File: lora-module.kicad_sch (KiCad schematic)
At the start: 10 parts, among them J101 Conn_Coaxial, J102 Conn_ARM_SWD_TagConnect_TC203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, Q101 PMN48XP

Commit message: added teardrops, finishing touches
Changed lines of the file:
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@@
     (in_bom no) (on_board yes) (dnp no) (fields_autoplaced)
     (property "Reference" "J106" (at 45.72 116.5169 0)
-      (effects (font (size 1.27 1.27)))
+      (effects (font (size 1.27 1.27)) hide)
     )
     (property "Value" "~" (at 45.72 116.84 0)

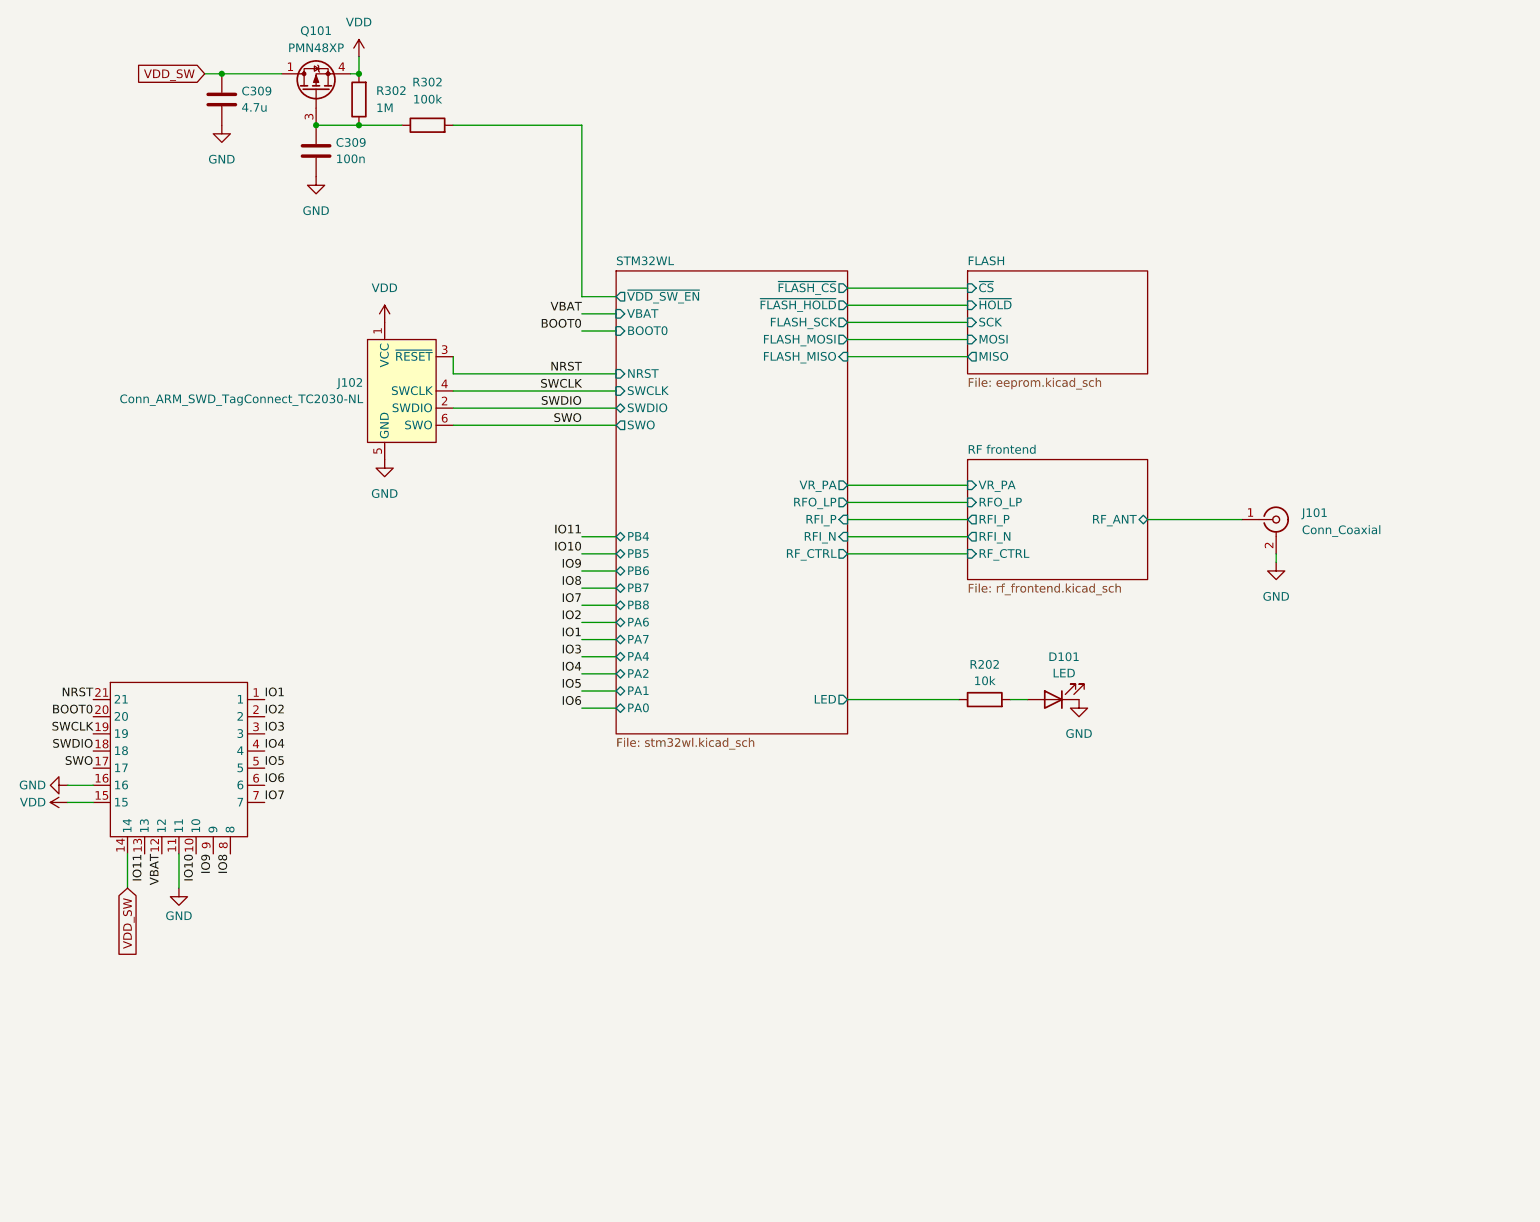
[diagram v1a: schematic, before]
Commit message: groundplane settings tweak
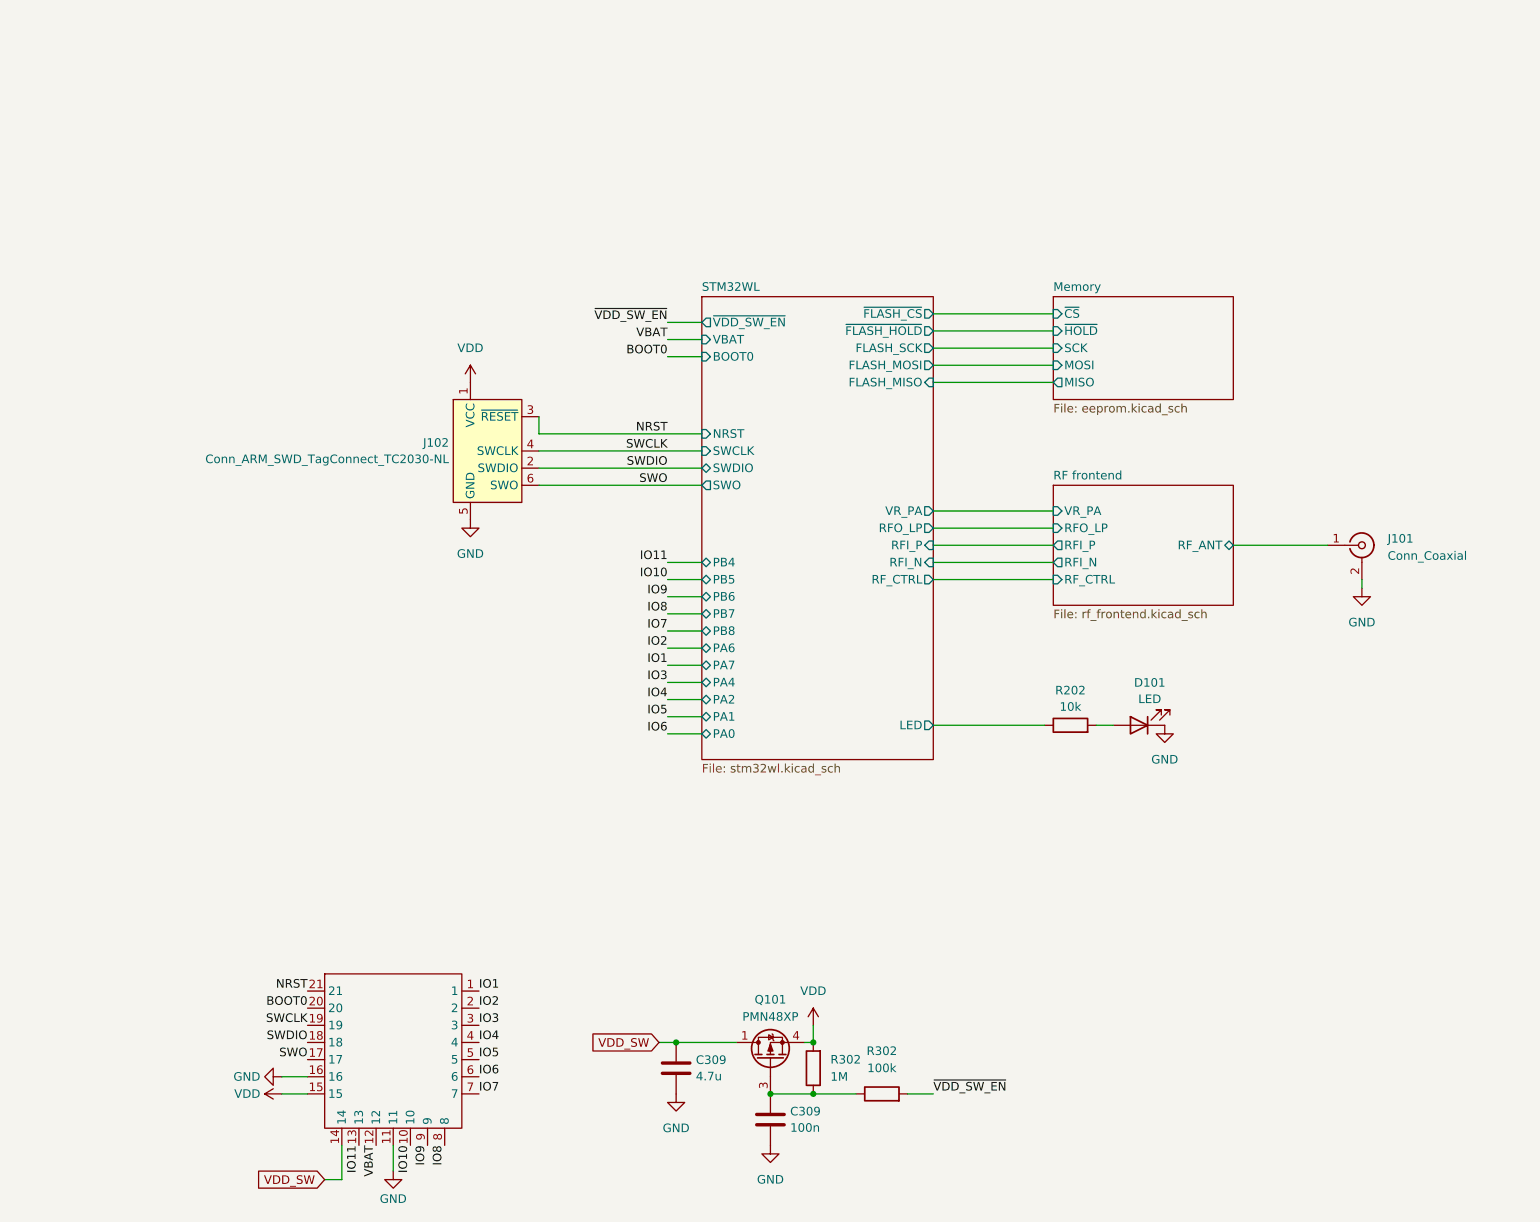
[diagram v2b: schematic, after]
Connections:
- net STM32WL/~{VDD_SW_EN} renamed ~{VDD_SW_EN}
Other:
- sheet FLASH renamed Memory
- moved on the sheet: C309, D101, J101, J102, Q101, R202, R302

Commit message: changed XO to TCXO
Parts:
- renumbered C309 to C101, C309 to C102, R302 to R101, R302 to R102, R202 to R103
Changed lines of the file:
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@@
   (symbol (lib_id "Device:C") (at 119.38 175.26 0) (unit 1)
     (in_bom yes) (on_board yes) (dnp no) (fields_autoplaced)
-    (property "Reference" "C309" (at 122.301 174.0479 0)
+    (property "Reference" "C101" (at 122.301 174.0479 0)
       (effects (font (size 1.27 1.27)) (justify left))
     )
@@
     (instances
       (project "lora-module"
-        (path "/30c7e509-35af-4828-996b-9681d057624f/8ccb3257-dd21-406f-b73b-aadedfaf4fa0"
-          (reference "C309") (unit 1)
-        )
-        (path "/30c7e509-35af-4828-996b-9681d057624f/93ed2c4d-2004-4e0b-a952-c18d2f9b026d"
-          (reference "C212") (unit 1)
-        )
         (path "/30c7e509-35af-4828-996b-9681d057624f"
           (reference "C101") (unit 1)
@@
   (symbol (lib_id "Device:C") (at 133.35 182.88 0) (unit 1)
     (in_bom yes) (on_board yes) (dnp no) (fields_autoplaced)
-    (property "Reference" "C309" (at 136.271 181.6679 0)
+    (property "Reference" "C102" (at 136.271 181.6679 0)
       (effects (font (size 1.27 1.27)) (justify left))
     )
@@
     (instances
       (project "lora-module"
-        (path "/30c7e509-35af-4828-996b-9681d057624f/8ccb3257-dd21-406f-b73b-aadedfaf4fa0"
-          (reference "C309") (unit 1)
-        )
         (path "/30c7e509-35af-4828-996b-9681d057624f"
           (reference "C102") (unit 1)
@@
   (symbol (lib_id "Device:R") (at 149.86 179.07 90) (unit 1)
     (in_bom yes) (on_board yes) (dnp no) (fields_autoplaced)
-    (property "Reference" "R302" (at 149.86 172.72 90)
+    (property "Reference" "R102" (at 149.86 172.72 90)
       (effects (font (size 1.27 1.27)))
     )
@@
     (instances
       (project "lora-module"
-        (path "/30c7e509-35af-4828-996b-9681d057624f/8ccb3257-dd21-406f-b73b-aadedfaf4fa0"
-          (reference "R302") (unit 1)
-        )
         (path "/30c7e509-35af-4828-996b-9681d057624f"
           (reference "R102") (unit 1)
@@
   (symbol (lib_id "Device:R") (at 139.7 175.26 180) (unit 1)
     (in_bom yes) (on_board yes) (dnp no) (fields_autoplaced)
-    (property "Reference" "R302" (at 142.24 173.99 0)
+    (property "Reference" "R101" (at 142.24 173.99 0)
       (effects (font (size 1.27 1.27)) (justify right))
     )
@@
     (instances
       (project "lora-module"
-        (path "/30c7e509-35af-4828-996b-9681d057624f/8ccb3257-dd21-406f-b73b-aadedfaf4fa0"
-          (reference "R302") (unit 1)
-        )
         (path "/30c7e509-35af-4828-996b-9681d057624f"
           (reference "R101") (unit 1)
@@
   (symbol (lib_id "Device:R") (at 177.8 124.46 90) (unit 1)
     (in_bom yes) (on_board yes) (dnp no) (fields_autoplaced)
-    (property "Reference" "R202" (at 177.8 119.2997 90)
+    (property "Reference" "R103" (at 177.8 119.2997 90)
       (effects (font (size 1.27 1.27)))
     )
@@
     (instances
       (project "lora-module"
-        (path "/30c7e509-35af-4828-996b-9681d057624f/93ed2c4d-2004-4e0b-a952-c18d2f9b026d"
-          (reference "R202") (unit 1)
-        )
         (path "/30c7e509-35af-4828-996b-9681d057624f"
           (reference "R103") (unit 1)

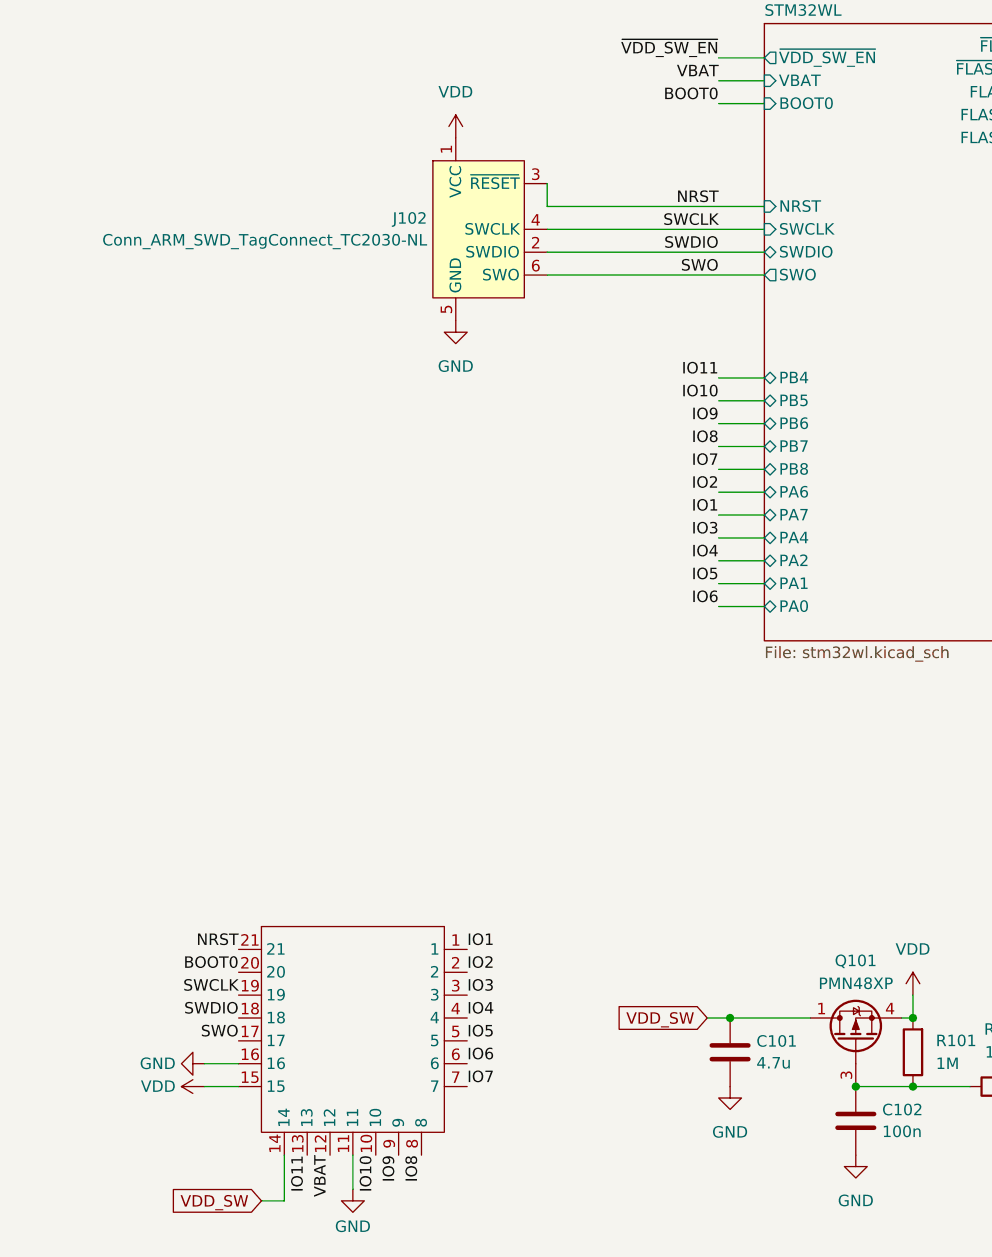
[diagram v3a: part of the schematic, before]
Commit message: module pinout change
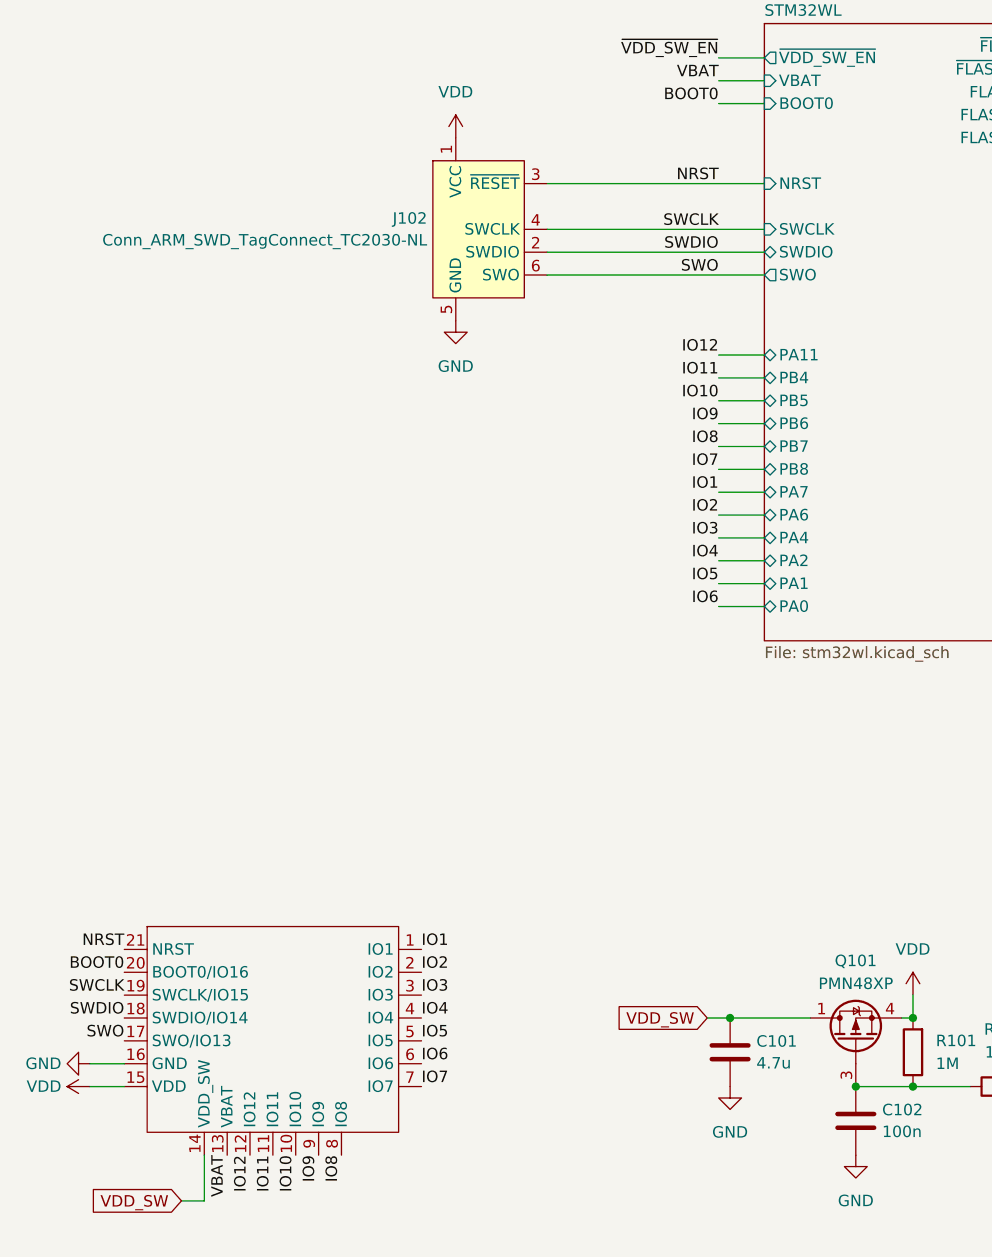
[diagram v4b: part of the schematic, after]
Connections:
- net GND: no longer J106.11
- net IO11: now also J106.11 (IO11); no longer J106.13
- net VBAT: now also J106.13 (VBAT); no longer J106.12
- new net IO12: J106.12 (IO12)
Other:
- sheet STM32WL ports: added PA11; removed none

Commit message: bom update and other tweaks
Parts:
- J101: value Conn_Coaxial -> U.FL-R-SMT-1(01)
- Q101: value PMN48XP -> PMN48XP,115
